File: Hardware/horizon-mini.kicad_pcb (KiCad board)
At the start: 2 copper layers, 34 x 34 mm, 79 parts, among them J2 Conn_01x02_Pin, J3 Micro_SD_Card_Det1, J7 USB_C_Receptacle_USB2.0_16P, J8 Conn_02x03_Counter_Clockwise, Q10 DMG2301L, U1 TPS82130, U16 AP2112K-3.3, U2 TPS61092, U3 LTC4412xS6, U5 ATSAMD21G18A-A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

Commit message: please liam fix decop caps
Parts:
- moved C7 1.75 mm to (137.6, 119.8)
- moved C11 1.75 mm to (137.6, 116.9)
- moved C8 1.75 mm to (137.6, 118.8)
- moved C9 1.75 mm to (137.6, 117.8)
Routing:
- net +3.3V: track 112.3 -> 108.4 mm
- net GND: track 105.7 -> 103.0 mm, vias 39 -> 35
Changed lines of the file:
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@@
 	(footprint "Capacitor_SMD:C_0402_1005Metric"
 		(layer "F.Cu")
-		(at 139.1825 119.01968)
+		(at 137.6 119.76357)
 		(descr "Capacitor SMD 0402 (1005 Metric), square (rectangular) end terminal, IPC-7351 nominal, (Body size source: IPC-SM-782 page 76, https://www.pcb-3d.com/wordpress/wp-content/uploads/ipc-sm-782a_amendment_1_and_2.pdf), generated with kicad-footprint-generator")
 		(tags "capacitor")
@@
 	(footprint "Capacitor_SMD:C_0402_1005Metric"
 		(layer "F.Cu")
-		(at 139.1825 117.083363)
+		(at 137.6 117.827253)
 		(descr "Capacitor SMD 0402 (1005 Metric), square (rectangular) end terminal, IPC-7351 nominal, (Body size source: IPC-SM-782 page 76, https://www.pcb-3d.com/wordpress/wp-content/uploads/ipc-sm-782a_amendment_1_and_2.pdf), generated with kicad-footprint-generator")
 		(tags "capacitor")
@@
 	(footprint "Capacitor_SMD:C_0402_1005Metric"
 		(layer "F.Cu")
-		(at 139.1825 116.119793)
+		(at 137.6 116.863683)
 		(descr "Capacitor SMD 0402 (1005 Metric), square (rectangular) end terminal, IPC-7351 nominal, (Body size source: IPC-SM-782 page 76, https://www.pcb-3d.com/wordpress/wp-content/uploads/ipc-sm-782a_amendment_1_and_2.pdf), generated with kicad-footprint-generator")
 		(tags "capacitor")
@@
 	(footprint "Capacitor_SMD:C_0402_1005Metric"
 		(layer "F.Cu")
-		(at 139.1825 118.05611)
+		(at 137.6 118.8)
 		(descr "Capacitor SMD 0402 (1005 Metric), square (rectangular) end terminal, IPC-7351 nominal, (Body size source: IPC-SM-782 page 76, https://www.pcb-3d.com/wordpress/wp-content/uploads/ipc-sm-782a_amendment_1_and_2.pdf), generated with kicad-footprint-generator")
 		(tags "capacitor")
@@
 	)
 	(segment
-		(start 139.6625 116.119793)
-		(end 139.6625 117.083363)
-		(width 0.4)
-		(layer "F.Cu")
-		(net 1)
-	)
-	(segment
 		(start 156.003876 117.747383)
 		(end 155.7932 117.536707)
@@
 	)
 	(segment
-		(start 139.6625 117.083363)
-		(end 139.6625 118.05611)
-		(width 0.4)
-		(layer "F.Cu")
-		(net 1)
-	)
-	(segment
 		(start 153.220573 106.502854)
 		(end 152.658866 105.941147)
@@
 	)
 	(segment
-		(start 139.67448 115.156223)
-		(end 139.67448 116.107813)
-		(width 0.4)
-		(layer "F.Cu")
-		(net 1)
-	)
-	(segment
 		(start 142.307937 114.814848)
 		(end 141.52 114.814848)
@@
 	)
 	(segment
-		(start 139.67448 116.107813)
-		(end 139.6625 116.119793)
-		(width 0.2)
-		(layer "F.Cu")
-		(net 1)
-	)
-	(segment
 		(start 157.1307 119.159349)
 		(end 157.1307 117.747383)
@@
 	)
 	(segment
-		(start 139.6625 118.05611)
-		(end 139.6625 119.01968)
-		(width 0.4)
-		(layer "F.Cu")
-		(net 1)
-	)
-	(segment
 		(start 150.1825 111.977348)
 		(end 150.1825 109.940285)
@@
 	)
 	(segment
-		(start 138.7025 118.05611)
-		(end 138.066675 118.05611)
-		(width 0.2)
-		(layer "F.Cu")
-		(net 2)
-	)
-	(segment
 		(start 154.176661 107.392428)
 		(end 154.176661 107.515354)
@@
 	)
 	(segment
-		(start 138.7025 117.083363)
-		(end 138.039422 117.083363)
-		(width 0.2)
-		(layer "F.Cu")
-		(net 2)
-	)
-	(segment
 		(start 157.896522 123.38699)
 		(end 157.896522 123.109918)
@@
 	)
 	(segment
-		(start 138.7025 116.119793)
-		(end 138.002992 116.119793)
-		(width 0.2)
-		(layer "F.Cu")
-		(net 2)
-	)
-	(segment
 		(start 169.369485 117.430515)
 		(end 169.3865 117.4135)
@@
 	)
 	(segment
-		(start 138.7025 119.01968)
-		(end 138.011895 119.01968)
-		(width 0.2)
-		(layer "F.Cu")
-		(net 2)
-	)
-	(segment
 		(start 145.4325 118.177502)
 		(end 145.533513 118.076489)
@@
 	)
 	(via
-		(at 138.002992 116.119793)
-		(size 0.45)
-		(drill 0.2)
-		(layers "F.Cu" "B.Cu")
-		(net 2)
-	)
-	(via
 		(at 156.2 108)
 		(size 0.45)
@@
 	)
 	(via
-		(at 138.039422 117.083363)
-		(size 0.45)
-		(drill 0.2)
-		(layers "F.Cu" "B.Cu")
-		(net 2)
-	)
-	(via
 		(at 162.25 114)
 		(size 0.45)
@@
 	)
 	(via
-		(at 138.066675 118.05611)
-		(size 0.45)
-		(drill 0.2)
-		(layers "F.Cu" "B.Cu")
-		(net 2)
-	)
-	(via
 		(at 142.070364 126.047776)
 		(size 0.45)
@@
 		(size 0.45)
 		(drill 0.2)
-		(layers "F.Cu" "B.Cu")
-		(net 2)
-	)
-	(via
-		(at 138.011895 119.01968)
-		(size 0.45)
-		(drill 0.2)

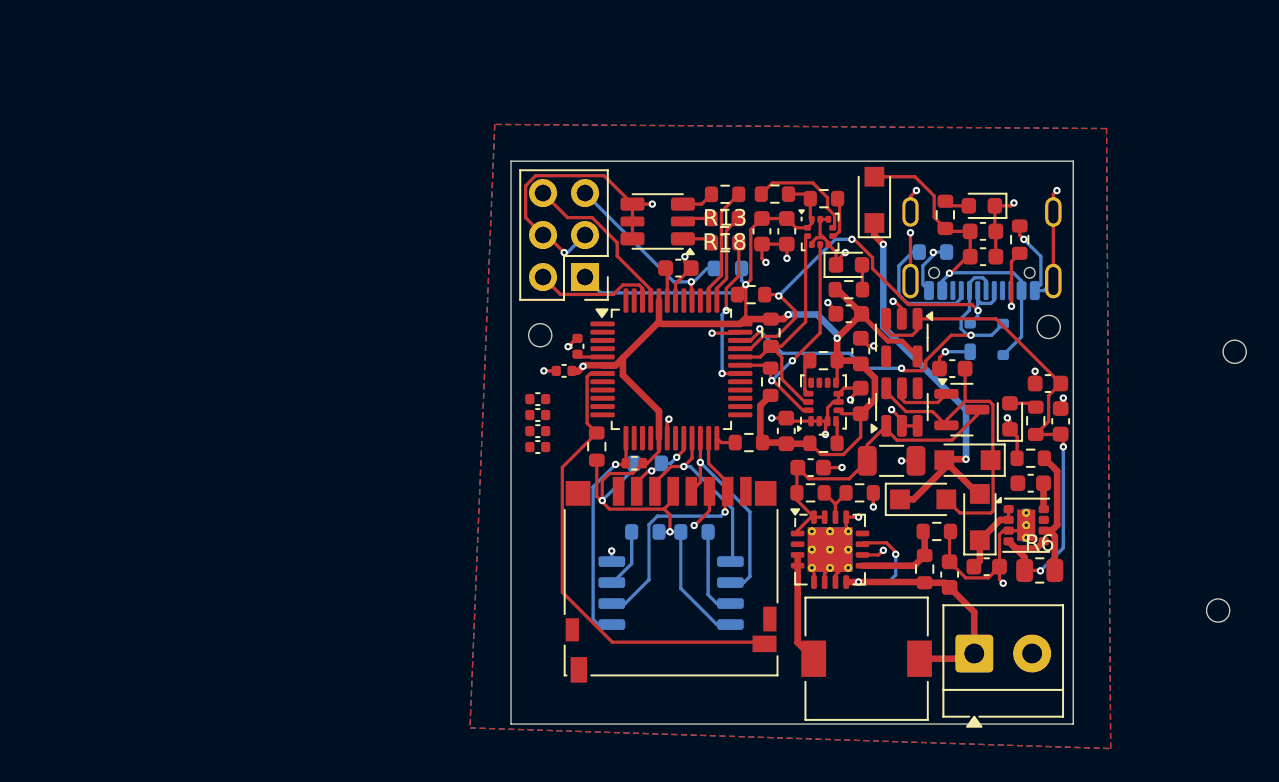
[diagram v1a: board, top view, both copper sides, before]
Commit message: fixed decop caps schematic and routes (plz check my work scooter)
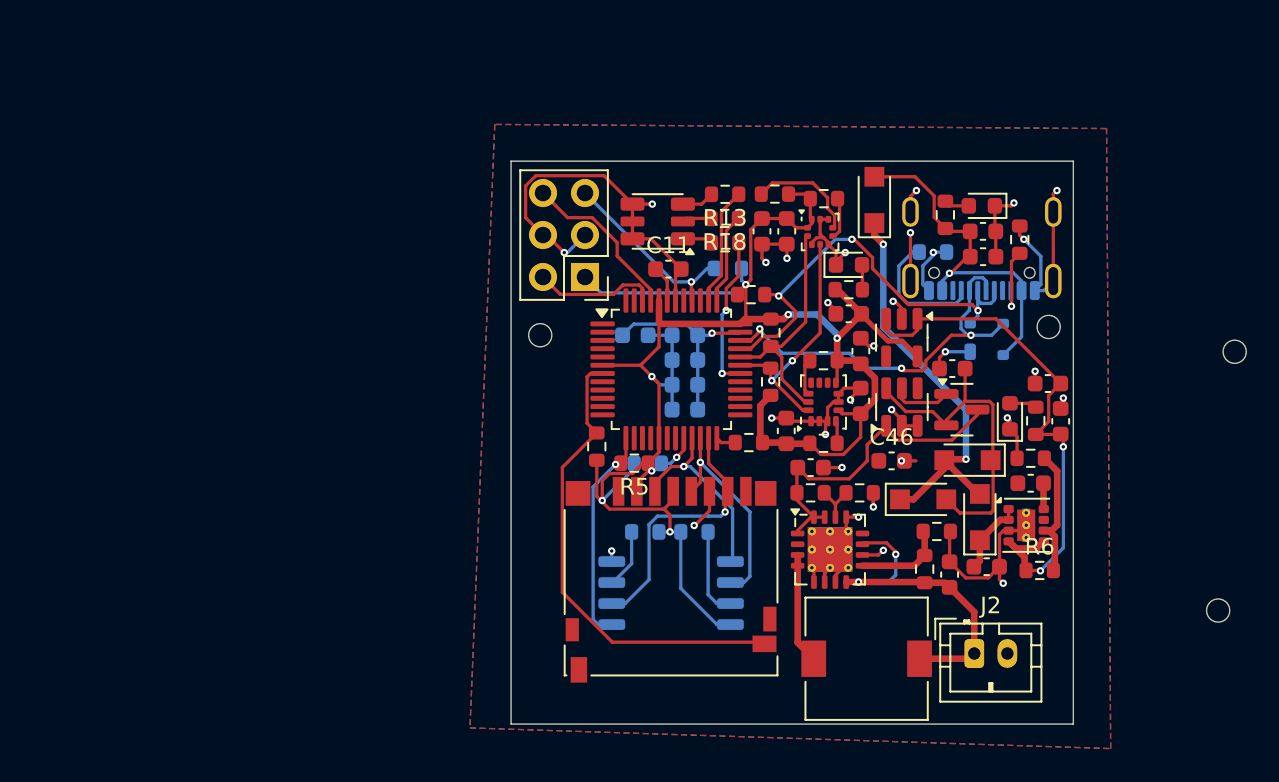
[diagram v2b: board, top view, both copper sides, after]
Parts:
- removed C78: 100nF, Capacitor_SMD:C_0402_1005Metric
- C11: value 100nF -> 1uF; footprint Capacitor_SMD:C_0402_1005Metric -> Capacitor_SMD:C_0603_1608Metric
- C12, C7: value 100nF -> 10uF; footprint Capacitor_SMD:C_0402_1005Metric -> Capacitor_SMD:C_0603_1608Metric; moved to B.Cu
- C46: footprint Capacitor_SMD:C_1206_3216Metric -> Capacitor_SMD:C_0603_1608Metric
- C6: moved to B.Cu
- C8, C9: footprint Capacitor_SMD:C_0402_1005Metric -> Capacitor_SMD:C_0603_1608Metric; moved to B.Cu
- J2: footprint TerminalBlock_MetzConnect:TerminalBlock_MetzConnect_Type059_RT06302HBWC_1x02_P3.50mm_Horizontal -> Connector_JST:JST_PH_B2B-PH-K_1x02_P2.00mm_Vertical
- R5: footprint Resistor_SMD:R_0402_1005Metric -> Resistor_SMD:R_0603_1608Metric
- R6: footprint Resistor_SMD:R_0805_2012Metric -> Resistor_SMD:R_0603_1608Metric
- moved C7 11.2 mm to (146.5, 113.0)
- moved C11 11.1 mm to (145.5, 109.0)
- moved C8 9.88 mm to (146.5, 114.5)
- moved C9 9.09 mm to (146.5, 116.0)
- moved C12 7.67 mm to (146.5, 117.5)
- moved C6 4.82 mm to (143.5, 113.0)
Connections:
- C1 pad 1: +3.3V -> VDDANA
- C11 pad 1: GND -> VDDCORE
- C11 pad 2: +3.3V -> GND
- C12 pad 1: GND -> VDDANA
- C12 pad 2: +3.3V -> GND
- C2 pad 2: +3.3V -> VDDANA
- C3 pad 2: +3.3V -> VDDANA
- C4 pad 2: +3.3V -> VDDANA
- C47 pad 1: +3.3V -> VDDANA
- C5 pad 2: +3.3V -> VDDANA
- C6 pad 1: GND -> VDDANA
- C6 pad 2: Net-(U5-VDDCORE) -> GND
- C7 pad 1: GND -> VDDANA
- C7 pad 2: +3.3V -> GND
- C8 pad 1: GND -> VDDANA
- C8 pad 2: +3.3V -> GND
- C9 pad 1: GND -> VDDANA
- C9 pad 2: +3.3V -> GND
- D14 pad 2: D+ DMCU-2 -> Net-(D14-I/O1)
- D14 pad 3: D- DMCU-2 -> Net-(D14-I/O2)
- J3 pad 4: +3.3V -> VDDANA
- J7 pad A6: D+ DMCU-2 -> Net-(D14-I/O1)
- J7 pad A7: D- DMCU-2 -> Net-(D14-I/O2)
- J7 pad B6: D+ DMCU-2 -> Net-(D14-I/O1)
- J7 pad B7: D- DMCU-2 -> Net-(D14-I/O2)
- J8 pad 1: +3.3V -> VDDANA
- R11 pad 1: +3.3V -> VDDANA
- R12 pad 2: +3.3V -> VDDANA
- R14 pad 1: +3.3V -> VDDANA
- R2 pad 1: +3.3V -> VDDANA
- R20 pad 2: +3.3V -> VDDANA
- R21 pad 1: +3.3V -> VDDANA
- R22 pad 1: +3.3V -> VDDANA
- R23 pad 1: +3.3V -> VDDANA
- R24 pad 2: +3.3V -> VDDANA
- R25 pad 1: +3.3V -> VDDANA
- R26 pad 2: +3.3V -> VDDANA
- R27 pad 2: +3.3V -> VDDANA
- R28 pad 1: +3.3V -> VDDANA
- R29 pad 1: +3.3V -> VDDANA
- R5 pad 1: +3.3V -> VDDANA
- U16 pad 5: +3.3V -> VDDANA
- U5 pad 17: +3.3V -> VDDANA
- U5 pad 36: +3.3V -> VDDANA
- U5 pad 43: Net-(U5-VDDCORE) -> VDDCORE
- U5 pad 44: +3.3V -> VDDANA
- U5 pad 5: Net-(U5-GNDANA) -> GND
- U5 pad 6: +3.3V -> VDDANA
- U6 pad 8: +3.3V -> VDDANA
- U7 pad 1: +3.3V -> VDDANA
- U7 pad 10: +3.3V -> VDDANA
- U9 pad 5: +3.3V -> VDDANA
- U9 pad 8: +3.3V -> VDDANA
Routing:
- net VDDANA: track 0.00 -> 113.6 mm, vias 0 -> 6
- net +3.3V: track 108.4 -> 0.00 mm, vias 6 -> 0
- net GND: track 103.0 -> 112.2 mm, vias 35 -> 31
- net VDDCORE: track 0.00 -> 2.20 mm
- net Net-(U5-VDDCORE): track 2.01 -> 0.00 mm
- net Net-(U5-GNDANA): track 1.59 -> 0.00 mm

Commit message: forgot to push
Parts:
- added C78: 100nF, Capacitor_SMD:C_0402_1005Metric, F.Cu at (140.0, 113.7)
- C11: value 1uF -> 10uF; footprint Capacitor_SMD:C_0603_1608Metric -> Capacitor_SMD:C_0402_1005Metric
- C12: value 10uF -> 100nF; footprint Capacitor_SMD:C_0603_1608Metric -> Capacitor_SMD:C_0402_1005Metric; moved to F.Cu
- C46: footprint Capacitor_SMD:C_0603_1608Metric -> Capacitor_SMD:C_1206_3216Metric
- C6: moved to F.Cu
- C7: value 10uF -> 100nF; footprint Capacitor_SMD:C_0603_1608Metric -> Capacitor_SMD:C_0402_1005Metric
- C8, C9: footprint Capacitor_SMD:C_0603_1608Metric -> Capacitor_SMD:C_0402_1005Metric
- J2: footprint Connector_JST:JST_PH_B2B-PH-K_1x02_P2.00mm_Vertical -> TerminalBlock_MetzConnect:TerminalBlock_MetzConnect_Type059_RT06302HBWC_1x02_P3.50mm_Horizontal
- R5: footprint Resistor_SMD:R_0603_1608Metric -> Resistor_SMD:R_0402_1005Metric
- R6: footprint Resistor_SMD:R_0603_1608Metric -> Resistor_SMD:R_0805_2012Metric
- moved C11 9.50 mm to (139.2, 116.1)
- moved C12 7.67 mm to (139.2, 115.2)
- moved C6 4.82 mm to (146.1, 108.9)
- moved C7 4.00 mm to (144.4, 109.6)
- moved C9 2.64 mm to (144.4, 117.6)
- moved C8 2.21 mm to (147.2, 112.4)
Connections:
- C1 pad 1: VDDANA -> +3.3V
- C11 pad 1: VDDCORE -> GND
- C11 pad 2: GND -> +3.3V
- C12 pad 1: VDDANA -> GND
- C12 pad 2: GND -> +3.3V
- C2 pad 2: VDDANA -> +3.3V
- C3 pad 2: VDDANA -> +3.3V
- C4 pad 2: VDDANA -> +3.3V
- C47 pad 1: VDDANA -> +3.3V
- C5 pad 2: VDDANA -> +3.3V
- C6 pad 1: VDDANA -> GND
- C6 pad 2: GND -> Net-(U5-VDDCORE)
- C7 pad 1: VDDANA -> GND
- C7 pad 2: GND -> +3.3V
- C8 pad 1: VDDANA -> GND
- C8 pad 2: GND -> +3.3V
- C9 pad 1: VDDANA -> GND
- C9 pad 2: GND -> +3.3V
- D14 pad 2: Net-(D14-I/O1) -> D+ DMCU-2
- D14 pad 3: Net-(D14-I/O2) -> D- DMCU-2
- J3 pad 4: VDDANA -> +3.3V
- J7 pad A6: Net-(D14-I/O1) -> D+ DMCU-2
- J7 pad A7: Net-(D14-I/O2) -> D- DMCU-2
- J7 pad B6: Net-(D14-I/O1) -> D+ DMCU-2
- J7 pad B7: Net-(D14-I/O2) -> D- DMCU-2
- J8 pad 1: VDDANA -> +3.3V
- R11 pad 1: VDDANA -> +3.3V
- R12 pad 2: VDDANA -> +3.3V
- R14 pad 1: VDDANA -> +3.3V
- R2 pad 1: VDDANA -> +3.3V
- R20 pad 2: VDDANA -> +3.3V
- R21 pad 1: VDDANA -> +3.3V
- R22 pad 1: VDDANA -> +3.3V
- R23 pad 1: VDDANA -> +3.3V
- R24 pad 2: VDDANA -> +3.3V
- R25 pad 1: VDDANA -> +3.3V
- R26 pad 2: VDDANA -> +3.3V
- R27 pad 2: VDDANA -> +3.3V
- R28 pad 1: VDDANA -> +3.3V
- R29 pad 1: VDDANA -> +3.3V
- R5 pad 1: VDDANA -> +3.3V
- U16 pad 5: VDDANA -> +3.3V
- U5 pad 17: VDDANA -> +3.3V
- U5 pad 36: VDDANA -> +3.3V
- U5 pad 43: VDDCORE -> Net-(U5-VDDCORE)
- U5 pad 44: VDDANA -> +3.3V
- U5 pad 5: GND -> Net-(U5-GNDANA)
- U5 pad 6: VDDANA -> +3.3V
- U6 pad 8: VDDANA -> +3.3V
- U7 pad 1: VDDANA -> +3.3V
- U7 pad 10: VDDANA -> +3.3V
- U9 pad 5: VDDANA -> +3.3V
- U9 pad 8: VDDANA -> +3.3V
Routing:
- net +3.3V: track 0.00 -> 113.9 mm, vias 0 -> 8
- net VDDANA: track 113.6 -> 0.00 mm, vias 6 -> 0
- net GND: track 112.2 -> 107.5 mm, vias 31 -> 37
- net VDDCORE: track 2.20 -> 0.00 mm
- net Net-(U5-VDDCORE): track 0.00 -> 2.01 mm
- net Net-(U5-GNDANA): track 0.00 -> 1.59 mm

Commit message: submission time!
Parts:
- removed the REF** at (178.8, 129.7)
- removed the REF** at (179.8, 114.0)
- moved U6 0.41 mm to (145.7, 129.0)
- moved J3 0.41 mm to (145.7, 128.2)
- moved R11 0.41 mm to (144.1, 125.3)
- moved R2 0.41 mm to (147.1, 125.3)
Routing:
- net GND: track 107.5 -> 108.7 mm
- net MOSI TMCU: track 11.8 -> 12.7 mm
- net +3.3V: track 113.9 -> 114.5 mm

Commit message: the board has been stitched!
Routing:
- net POWAAAA: track 20.1 -> 21.0 mm
- net GND: vias 37 -> 107
- net (no net): vias 0 -> 2

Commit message: add prod files
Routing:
- net GND: track 108.7 -> 108.5 mm, vias 107 -> 126
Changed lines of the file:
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@@
 	)
 	(via
+		(at 137.5 134.25)
+		(size 0.55)
+		(drill 0.3)
+		(layers "F.Cu" "B.Cu")
+		(free yes)
+		(net 2)
+	)
+	(via
 		(at 140 117)
 		(size 0.55)
@@
 	)
 	(via
+		(at 157.5 132.25)
+		(size 0.55)
+		(drill 0.3)
+		(layers "F.Cu" "B.Cu")
+		(free yes)
+		(net 2)
+	)
+	(via
+		(at 137.5 118.25)
+		(size 0.55)
+		(drill 0.3)
+		(layers "F.Cu" "B.Cu")
+		(free yes)
+		(net 2)
+	)
+	(via
 		(at 148.2 133)
 		(size 0.55)
@@
 	)
 	(via
+		(at 165.5 134.25)
+		(size 0.55)
+		(drill 0.3)
+		(layers "F.Cu" "B.Cu")
+		(free yes)
+		(net 2)
+	)
+	(via
 		(at 150 133)
 		(size 0.55)
@@
 	)
 	(via
+		(at 167.5 132.25)
+		(size 0.55)
+		(drill 0.3)
+		(layers "F.Cu" "B.Cu")
+		(free yes)
+		(net 2)
+	)
+	(via
 		(at 161.306283 113.311337)
 		(size 0.55)
@@
 	)
 	(via
+		(at 143.5 134.25)
+		(size 0.55)
+		(drill 0.3)
+		(layers "F.Cu" "B.Cu")
+		(free yes)
+		(net 2)
+	)
+	(via
 		(at 143.4 114.8)
 		(size 0.55)
@@
 	)
 	(via
+		(at 145.5 134.25)
+		(size 0.55)
+		(drill 0.3)
+		(layers "F.Cu" "B.Cu")
+		(free yes)
+		(net 2)
+	)
+	(via
 		(at 149 124.8)
 		(size 0.55)
@@
 	)
 	(via
+		(at 137.5 132.25)
+		(size 0.55)
+		(drill 0.3)
+		(layers "F.Cu" "B.Cu")
+		(free yes)
+		(net 2)
+	)
+	(via
+		(at 141.5 134.25)
+		(size 0.55)
+		(drill 0.3)
+		(layers "F.Cu" "B.Cu")
+		(free yes)
+		(net 2)
+	)
+	(via
 		(at 156.2 108)
 		(size 0.55)
@@
 	)
 	(via
+		(at 167.5 130.25)
+		(size 0.55)
+		(drill 0.3)
+		(layers "F.Cu" "B.Cu")
+		(free yes)
+		(net 2)
+	)
+	(via
 		(at 169.199126 116.809193)
 		(size 0.55)
@@
 	)
 	(via
+		(at 167.5 134.25)
+		(size 0.55)
+		(drill 0.3)
+		(layers "F.Cu" "B.Cu")
+		(free yes)
+		(net 2)
+	)
+	(via
 		(at 143.266055 117.623731)
 		(size 0.55)
@@
 	)
 	(via
+		(at 157.5 134.25)
+		(size 0.55)
+		(drill 0.3)
+		(layers "F.Cu" "B.Cu")
+		(free yes)
+		(net 2)
+	)
+	(via
 		(at 159.598225 120.598225)
 		(size 0.55)
@@
 	)
 	(via
+		(at 157.5 130.25)
+		(size 0.55)
+		(drill 0.3)
+		(layers "F.Cu" "B.Cu")
+		(free yes)
+		(net 2)
+	)
+	(via
 		(at 163.193037 125.79833)
 		(size 0.55)
@@
 	)
 	(via
+		(at 151.5 134.25)
+		(size 0.55)
+		(drill 0.3)
+		(layers "F.Cu" "B.Cu")
+		(free yes)
+		(net 2)
+	)
+	(via
 		(at 143.8 132.8)
 		(size 0.55)
@@
 	)
 	(via
+		(at 155.5 130.25)
+		(size 0.55)
+		(drill 0.3)
+		(layers "F.Cu" "B.Cu")
+		(free yes)
+		(net 2)
+	)
+	(via
 		(at 162.4 121.8)
 		(size 0.55)
@@
 	)
 	(via
+		(at 145.5 130.25)
+		(size 0.55)
+		(drill 0.3)
+		(layers "F.Cu" "B.Cu")
+		(free yes)
+		(net 2)
+	)
+	(via
 		(at 154 131)
 		(size 0.55)
@@
 	)
 	(via
+		(at 159.5 130.25)
+		(size 0.55)
+		(drill 0.3)
+		(layers "F.Cu" "B.Cu")
+		(free yes)
+		(net 2)
+	)
+	(via
 		(at 152.497185 117.118708)
 		(size 0.55)
@@
 		(net 2)
 	)
-	(segment
-		(start 160.895249 109.933323)
-		(end 160.895249 108.796404)
-		(width 0.2)
-		(layer "B.Cu")
+	(via
+		(at 158.6 124.4)
+		(size 0.55)
+		(drill 0.3)
+		(layers "F.Cu" "B.Cu")
+		(free yes)
+		(net 2)
+	)
+	(via
+		(at 167.4 121.2)
+		(size 0.55)
+		(drill 0.3)
+		(layers "F.Cu" "B.Cu")
+		(free yes)
 		(net 2)
 	)
@@
 	)
 	(segment
-		(start 167.661249 110.299323)
-		(end 168.027249 109.933323)
+		(start 161.261249 110.299323)
+		(end 160.895249 109.933323)
 		(width 0.2)
 		(layer "B.Cu")
@@
 	)
 	(segment
-		(start 142.075 127.099715)
-		(end 142.075 126.462127)
+		(start 167.661249 110.299323)
+		(end 168.027249 109.933323)
 		(width 0.2)
 		(layer "B.Cu")
@@
 	)
 	(segment
-		(start 161.261249 110.299323)
-		(end 160.895249 109.933323)
+		(start 142.075 127.099715)
+		(end 142.075 126.462127)
 		(width 0.2)
 		(layer "B.Cu")
@@
 	)
 	(segment
-		(start 162.325 107.969011)
-		(end 161.545265 107.969011)
-		(width 0.2)
-		(layer "B.Cu")
-		(net 2)
-	)
-	(segment
 		(start 168.027249 108.227249)
 		(end 167 107.2)
@@
 	)
 	(segment
-		(start 161.522262 108.169391)
-		(end 161.522262 107.992014)
+		(start 167.661249 110.299323)
+		(end 168.206249 110.299323)
 		(width 0.2)
 		(layer "B.Cu")
@@
 	)
 	(segment
-		(start 167.661249 110.299323)
-		(end 168.206249 110.299323)
+		(start 161.870553 107.969011)
+		(end 162.325 107.969011)
 		(width 0.2)
 		(layer "B.Cu")
@@
 	)
 	(segment
-		(start 139.397785 108)
-		(end 140.4575 106.940285)
+		(start 160.895249 109.933323)
+		(end 160.895249 108.944315)
 		(width 0.2)
 		(layer "B.Cu")
@@
 	)
 	(segment
-		(start 143.289786 117.6)
-		(end 143.92 117.6)
+		(start 139.397785 108)
+		(end 140.4575 106.940285)
 		(width 0.2)
 		(layer "B.Cu")
@@
 	)
 	(segment
-		(start 161.545265 107.969011)
-		(end 161.522262 107.992014)
+		(start 143.289786 117.6)
+		(end 143.92 117.6)
 		(width 0.2)
 		(layer "B.Cu")
@@
 	)
 	(segment
-		(start 160.895249 108.796404)
-		(end 161.522262 108.169391)
+		(start 162.4 114)
+		(end 162.25 114)
 		(width 0.2)
 		(layer "B.Cu")
@@
 	)
 	(segment
-		(start 162.4 114)
-		(end 162.25 114)
+		(start 168.027249 109.933323)
+		(end 168.027249 108.227249)
 		(width 0.2)
 		(layer "B.Cu")
@@
 	)
 	(segment
-		(start 168.027249 109.933323)
-		(end 168.027249 108.227249)
+		(start 160.895249 108.944315)
+		(end 161.870553 107.969011)
 		(width 0.2)
 		(layer "B.Cu")
@@
 		)
 	)
+	(group "ViaStitching GND"
+		(members "301a81f7-42b6-43ee-a53e-f9c4cfee8e97" "34054aab-b82f-49d8-a669-3193ca905aa2"
+			"39d891e9-7dad-4535-9024-9e3378434e01" "3fc8ec77-80e5-4207-b93d-18e1bd245592"
+			"486ba199-a8e4-4a5b-b148-6a808537820f" "4c267cd9-09ff-42e2-a557-e04d06d4238d"
+			"58be397e-5bb1-40ea-a72e-308e41e14ef0" "65609c28-1c34-4f51-8698-f68fc2df6a20"
+			"689ba732-e0d4-4749-91f6-f9aa1e114a4e" "7029397c-f6b8-4fed-b092-8ac6a1fc0431"
+			"7e402b24-02e9-48ec-832a-1f4ae6ebe307" "813e41a5-83ab-44fe-86e0-7f7fe3bc2ade"
+			"84e91ba8-0150-4458-95d7-187cfd78c17e" "b9422b0a-ba39-47aa-bc7e-05e91cf38388"
+			"cbc36ecf-86db-4edf-b52d-40c24164e84a" "f050ce10-a556-486d-89ab-5425c1521a1b"
+			"f4670b8d-9103-407c-b267-5e77d49be8ec"
+		)
+	)

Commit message: wooooah, found an error.. all good now!
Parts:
- R15: moved to F.Cu
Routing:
- net Net-(J7-CC1): track 7.92 -> 9.69 mm, vias 0 -> 1
- net GND: track 108.5 -> 106.8 mm, vias 126 -> 127
